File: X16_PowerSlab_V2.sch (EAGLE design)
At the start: 41 parts, among them J1 CONN_796636-3, J2 CONN_796636-3, J3 CONN_ET60T

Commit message: updated board
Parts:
- removed COUT1, COUT2, COUT3: 150uF, SparkFun-Capacitors:10UF-POLAR-0603-6.3V-20%(TANT)
- added COUT4, COUT5, COUT6: 150uF, X15-Conversion-Parts-Library:C-TANTALUM(10UF_150UF)
- CIN1: value 180uF -> 150uF; device SparkFun-Capacitors:10UF-POLAR-0603-6.3V-20%(TANT) -> X15-Conversion-Parts-Library:C-TANTALUM(10UF_150UF)
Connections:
- net 5.2V: now also COUT4.+, COUT5.+, COUT6.+; no longer COUT1.+, COUT2.+, COUT3.+
- net GND: now also COUT4.-, COUT5.-, COUT6.-; no longer COUT1.-, COUT2.-, COUT3.-
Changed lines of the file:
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@@
 <part name="CIN2" library="SparkFun-Capacitors" library_urn="urn:adsk.eagle:library:510" deviceset="0.1UF" device="-0603-25V-(+80/-20%)" package3d_urn="urn:adsk.eagle:package:41385090/1" value="0.47uF"/>
 <part name="C2" library="SparkFun-Capacitors" library_urn="urn:adsk.eagle:library:510" deviceset="0.1UF" device="-0603-25V-(+80/-20%)" package3d_urn="urn:adsk.eagle:package:41385090/1" value="0.01uF"/>
-<part name="COUT1" library="SparkFun-Capacitors" library_urn="urn:adsk.eagle:library:510" deviceset="10UF-POLAR" device="-0603-6.3V-20%(TANT)" package3d_urn="urn:adsk.eagle:package:41385074/1" value="150uF"/>
-<part name="COUT2" library="SparkFun-Capacitors" library_urn="urn:adsk.eagle:library:510" deviceset="10UF-POLAR" device="-0603-6.3V-20%(TANT)" package3d_urn="urn:adsk.eagle:package:41385074/1" value="150uF"/>
-<part name="COUT3" library="SparkFun-Capacitors" library_urn="urn:adsk.eagle:library:510" deviceset="10UF-POLAR" device="-0603-6.3V-20%(TANT)" package3d_urn="urn:adsk.eagle:package:41385074/1" value="150uF"/>
-<part name="CIN1" library="SparkFun-Capacitors" library_urn="urn:adsk.eagle:library:510" deviceset="10UF-POLAR" device="-0603-6.3V-20%(TANT)" package3d_urn="urn:adsk.eagle:package:41385074/1" value="180uF"/>
 <part name="R1" library="SparkFun-Resistors" library_urn="urn:adsk.eagle:library:532" deviceset="RESISTOR" device="0603" package3d_urn="urn:adsk.eagle:package:41389018/1" value="1k"/>
 <part name="R2" library="SparkFun-Resistors" library_urn="urn:adsk.eagle:library:532" deviceset="RESISTOR" device="0603" package3d_urn="urn:adsk.eagle:package:41389018/1" value="3.32k"/>
@@
 <part name="TP6" library="SparkFun-Connectors" library_urn="urn:adsk.eagle:library:513" deviceset="TEST-POINT" device="3X5" package3d_urn="urn:adsk.eagle:package:38285/2"/>
 <part name="L1" library="X15-Conversion-Parts-Library" deviceset="HCMA1305" device="" package3d_urn="urn:adsk.eagle:package:24201702/2" value="15uH"/>
+<part name="COUT4" library="X15-Conversion-Parts-Library" deviceset="C-TANTALUM(10UF_150UF)" device="" package3d_urn="urn:adsk.eagle:package:25131320/3" value="150uF"/>
+<part name="COUT5" library="X15-Conversion-Parts-Library" deviceset="C-TANTALUM(10UF_150UF)" device="" package3d_urn="urn:adsk.eagle:package:25131320/3" value="150uF"/>
+<part name="COUT6" library="X15-Conversion-Parts-Library" deviceset="C-TANTALUM(10UF_150UF)" device="" package3d_urn="urn:adsk.eagle:package:25131320/3" value="150uF"/>
+<part name="CIN1" library="X15-Conversion-Parts-Library" deviceset="C-TANTALUM(10UF_150UF)" device="" package3d_urn="urn:adsk.eagle:package:25131320/3" value="150uF"/>
 </parts>
 <sheets>
@@
 <attribute name="VALUE" x="50.419" y="65.024" size="1.778" layer="96" font="vector" rot="R90"/>
 </instance>
-<instance part="COUT1" gate="G$1" x="66.04" y="50.8" smashed="yes">
-<attribute name="NAME" x="67.056" y="51.435" size="1.778" layer="95" font="vector"/>
-<attribute name="VALUE" x="67.056" y="46.609" size="1.778" layer="96" font="vector"/>
-</instance>
-<instance part="COUT2" gate="G$1" x="73.66" y="50.8" smashed="yes">
-<attribute name="NAME" x="74.676" y="51.435" size="1.778" layer="95" font="vector"/>
-<attribute name="VALUE" x="74.676" y="46.609" size="1.778" layer="96" font="vector"/>
-</instance>
-<instance part="COUT3" gate="G$1" x="81.28" y="50.8" smashed="yes">
-<attribute name="NAME" x="82.296" y="51.435" size="1.778" layer="95" font="vector"/>
-<attribute name="VALUE" x="82.296" y="46.609" size="1.778" layer="96" font="vector"/>
-</instance>
-<instance part="CIN1" gate="G$1" x="-60.96" y="66.04" smashed="yes">
-<attribute name="NAME" x="-59.944" y="66.675" size="1.778" layer="95" font="vector"/>
-<attribute name="VALUE" x="-59.944" y="61.849" size="1.778" layer="96" font="vector"/>
-</instance>
 <instance part="R1" gate="G$1" x="60.96" y="81.28" smashed="yes">
 <attribute name="NAME" x="60.96" y="82.804" size="1.778" layer="95" font="vector" align="bottom-center"/>
@@
 <attribute name="NAME" x="50.8" y="57.15" size="0.762" layer="95"/>
 <attribute name="VALUE" x="50.8" y="54.61" size="0.762" layer="96"/>
+</instance>
+<instance part="COUT4" gate="G$1" x="66.04" y="50.8" smashed="yes">
+<attribute name="NAME" x="67.056" y="51.435" size="0.762" layer="95"/>
+<attribute name="VALUE" x="67.056" y="46.609" size="0.762" layer="96"/>
+</instance>
+<instance part="COUT5" gate="G$1" x="73.66" y="50.8" smashed="yes">
+<attribute name="NAME" x="74.676" y="51.435" size="0.762" layer="95"/>
+<attribute name="VALUE" x="74.676" y="46.609" size="0.762" layer="96"/>
+</instance>
+<instance part="COUT6" gate="G$1" x="81.28" y="50.8" smashed="yes">
+<attribute name="NAME" x="82.296" y="51.435" size="0.762" layer="95"/>
+<attribute name="VALUE" x="82.296" y="46.609" size="0.762" layer="96"/>
+</instance>
+<instance part="CIN1" gate="G$1" x="-60.96" y="66.04" smashed="yes">
+<attribute name="NAME" x="-59.944" y="66.675" size="0.762" layer="95"/>
+<attribute name="VALUE" x="-59.944" y="61.849" size="0.762" layer="96"/>
 </instance>
 </instances>
@@
 <net name="5.2V" class="0">
 <segment>
-<pinref part="COUT1" gate="G$1" pin="+"/>
 <wire x1="66.04" y1="55.88" x2="73.66" y2="55.88" width="0.1524" layer="91"/>
 <wire x1="73.66" y1="55.88" x2="81.28" y2="55.88" width="0.1524" layer="91"/>
@@
 <wire x1="66.04" y1="53.34" x2="66.04" y2="55.88" width="0.1524" layer="91"/>
 <junction x="66.04" y="55.88"/>
-<pinref part="COUT2" gate="G$1" pin="+"/>
 <wire x1="73.66" y1="53.34" x2="73.66" y2="55.88" width="0.1524" layer="91"/>
 <junction x="73.66" y="55.88"/>
-<pinref part="COUT3" gate="G$1" pin="+"/>
 <wire x1="81.28" y1="53.34" x2="81.28" y2="55.88" width="0.1524" layer="91"/>
 <junction x="81.28" y="55.88"/>
@@
 <label x="86.36" y="55.88" size="1.778" layer="95" xref="yes"/>
 <pinref part="L1" gate="G$1" pin="2"/>
+<pinref part="COUT4" gate="G$1" pin="+"/>
+<pinref part="COUT5" gate="G$1" pin="+"/>
+<pinref part="COUT6" gate="G$1" pin="+"/>
 </segment>
 <segment>
@@
 <pinref part="CIN2" gate="G$1" pin="2"/>
 <wire x1="-48.26" y1="60.96" x2="-48.26" y2="43.18" width="0.1524" layer="91"/>
-<pinref part="CIN1" gate="G$1" pin="-"/>
 <wire x1="-60.96" y1="60.96" x2="-60.96" y2="43.18" width="0.1524" layer="91"/>
 <wire x1="-60.96" y1="43.18" x2="-48.26" y2="43.18" width="0.1524" layer="91"/>
-<pinref part="COUT3" gate="G$1" pin="-"/>
 <wire x1="-48.26" y1="43.18" x2="-27.94" y2="43.18" width="0.1524" layer="91"/>
 <wire x1="-27.94" y1="43.18" x2="-17.78" y2="43.18" width="0.1524" layer="91"/>
@@
 <wire x1="73.66" y1="43.18" x2="81.28" y2="43.18" width="0.1524" layer="91"/>
 <wire x1="81.28" y1="43.18" x2="81.28" y2="45.72" width="0.1524" layer="91"/>
-<pinref part="COUT1" gate="G$1" pin="-"/>
 <wire x1="66.04" y1="45.72" x2="66.04" y2="43.18" width="0.1524" layer="91"/>
 <junction x="66.04" y="43.18"/>
-<pinref part="COUT2" gate="G$1" pin="-"/>
 <wire x1="73.66" y1="45.72" x2="73.66" y2="43.18" width="0.1524" layer="91"/>
 <junction x="73.66" y="43.18"/>
@@
 <junction x="50.8" y="43.18"/>
 <label x="-17.78" y="40.64" size="1.778" layer="95" rot="R270" xref="yes"/>
+<pinref part="COUT4" gate="G$1" pin="-"/>
+<pinref part="COUT5" gate="G$1" pin="-"/>
+<pinref part="COUT6" gate="G$1" pin="-"/>
+<pinref part="CIN1" gate="G$1" pin="-"/>
 </segment>
 <segment>
@@
 <pinref part="CIN2" gate="G$1" pin="1"/>
 <wire x1="-48.26" y1="68.58" x2="-48.26" y2="71.12" width="0.1524" layer="91"/>
-<pinref part="CIN1" gate="G$1" pin="+"/>
 <wire x1="-60.96" y1="68.58" x2="-60.96" y2="71.12" width="0.1524" layer="91"/>
 <pinref part="U$2" gate="G$1" pin="VIN"/>
@@
 <wire x1="-60.96" y1="71.12" x2="-68.58" y2="71.12" width="0.1524" layer="91"/>
 <pinref part="D4" gate="G$1" pin="C"/>
-</segment>
-</net>
+<pinref part="CIN1" gate="G$1" pin="+"/>
+</segment>
+</net>

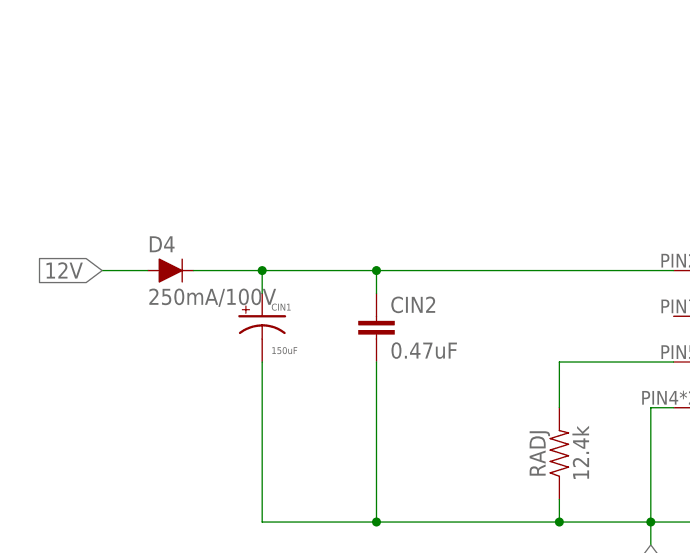
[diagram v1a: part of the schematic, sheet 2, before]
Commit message: finished polygons
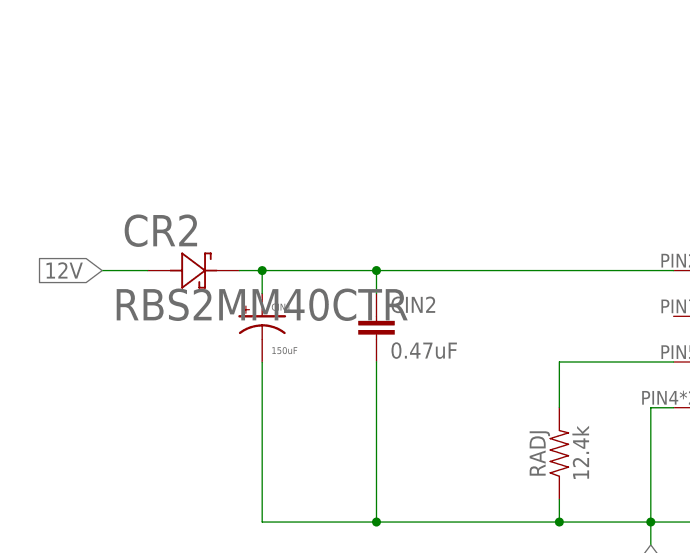
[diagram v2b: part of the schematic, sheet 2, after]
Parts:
- removed D4: 250mA/100V, SparkFun-DiscreteSemi:DIODE-BAS16J
- added CR2: RBS2MM40CTR, X16_Power_Slab:RBS2MM40CTR
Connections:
- net 12V: now also CR2.2; no longer D4.A
- net 48V_GND: now also U$3.RMCONT
- net VIN: now also CR2.1; no longer D4.C
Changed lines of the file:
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@@
 <part name="C4" library="SparkFun-Capacitors" library_urn="urn:adsk.eagle:library:510" deviceset="10UF-POLAR" device="-0603-6.3V-20%(TANT)" package3d_urn="urn:adsk.eagle:package:41385074/1" value="330uF"/>
 <part name="C7" library="SparkFun-Capacitors" library_urn="urn:adsk.eagle:library:510" deviceset="10UF-POLAR" device="-0603-6.3V-20%(TANT)" package3d_urn="urn:adsk.eagle:package:41385074/1" value="330uF"/>
-<part name="D4" library="SparkFun-DiscreteSemi" library_urn="urn:adsk.eagle:library:514" deviceset="DIODE" device="-BAS16J" package3d_urn="urn:adsk.eagle:package:38441/2" value="250mA/100V"/>
 <part name="U$6" library="X16_Power_Slab" deviceset="CONN_DISTRIBUTION_TO_CONVERSION" device=""/>
 <part name="48_TP" library="SparkFun-Connectors" library_urn="urn:adsk.eagle:library:513" deviceset="TEST-POINT" device="3X5" package3d_urn="urn:adsk.eagle:package:38285/2"/>
@@
 <part name="COUT6" library="X15-Conversion-Parts-Library" deviceset="C-TANTALUM(10UF_150UF)" device="" package3d_urn="urn:adsk.eagle:package:25131320/3" value="150uF"/>
 <part name="CIN1" library="X15-Conversion-Parts-Library" deviceset="C-TANTALUM(10UF_150UF)" device="" package3d_urn="urn:adsk.eagle:package:25131320/3" value="150uF"/>
+<part name="CR2" library="X16_Power_Slab" deviceset="RBS2MM40CTR" device=""/>
 </parts>
 <sheets>
@@
 </segment>
 <segment>
-<wire x1="12.7" y1="137.16" x2="5.08" y2="137.16" width="0.1524" layer="91"/>
+<wire x1="12.7" y1="137.16" x2="7.62" y2="137.16" width="0.1524" layer="91"/>
 <pinref part="U$3" gate="G$1" pin="48V_GND"/>
 <label x="5.08" y="137.16" size="1.778" layer="95"/>
+<pinref part="U$3" gate="G$1" pin="RMCONT"/>
+<wire x1="7.62" y1="137.16" x2="5.08" y2="137.16" width="0.1524" layer="91"/>
+<wire x1="12.7" y1="147.32" x2="7.62" y2="147.32" width="0.1524" layer="91"/>
+<wire x1="7.62" y1="147.32" x2="7.62" y2="137.16" width="0.1524" layer="91"/>
+<junction x="7.62" y="137.16"/>
 </segment>
 <segment>
@@
 <attribute name="VALUE" x="27.432" y="-3.175" size="1.778" layer="96" font="vector" rot="R180" align="top-left"/>
 </instance>
-<instance part="D4" gate="G$1" x="-71.12" y="71.12" smashed="yes">
-<attribute name="NAME" x="-73.66" y="73.152" size="1.778" layer="95" font="vector"/>
-<attribute name="VALUE" x="-73.66" y="69.088" size="1.778" layer="96" font="vector" align="top-left"/>
-</instance>
 <instance part="48_TP" gate="G$1" x="73.66" y="7.62" smashed="yes">
 <attribute name="NAME" x="71.12" y="10.16" size="1.778" layer="95" font="vector"/>
@@
 <attribute name="NAME" x="-59.944" y="66.675" size="0.762" layer="95"/>
 <attribute name="VALUE" x="-59.944" y="61.849" size="0.762" layer="96"/>
+</instance>
+<instance part="CR2" gate="A" x="-73.66" y="71.12" smashed="yes">
+<attribute name="VALUE" x="-77.5462" y="65.5828" size="3.4798" layer="96" ratio="10" rot="SR0"/>
+<attribute name="NAME" x="-76.4794" y="73.8124" size="3.4798" layer="95" ratio="10" rot="SR0"/>
 </instance>
 </instances>
@@
 <wire x1="-73.66" y1="71.12" x2="-78.74" y2="71.12" width="0.1524" layer="91"/>
 <label x="-78.74" y="71.12" size="1.778" layer="95" rot="R180" xref="yes"/>
-<pinref part="D4" gate="G$1" pin="A"/>
+<pinref part="CR2" gate="A" pin="2"/>
 </segment>
 </net>
@@
 <pinref part="U$2" gate="G$1" pin="VIN"/>
 <wire x1="-60.96" y1="71.12" x2="-48.26" y2="71.12" width="0.1524" layer="91"/>
-<junction x="-60.96" y="71.12"/>
 <junction x="-48.26" y="71.12"/>
 <wire x1="-48.26" y1="71.12" x2="-15.24" y2="71.12" width="0.1524" layer="91"/>
-<wire x1="-60.96" y1="71.12" x2="-68.58" y2="71.12" width="0.1524" layer="91"/>
-<pinref part="D4" gate="G$1" pin="C"/>
 <pinref part="CIN1" gate="G$1" pin="+"/>
-</segment>
-</net>
+<pinref part="CR2" gate="A" pin="1"/>
+<wire x1="-63.5" y1="71.12" x2="-60.96" y2="71.12" width="0.1524" layer="91"/>
+<junction x="-60.96" y="71.12"/>
+</segment>
+</net>

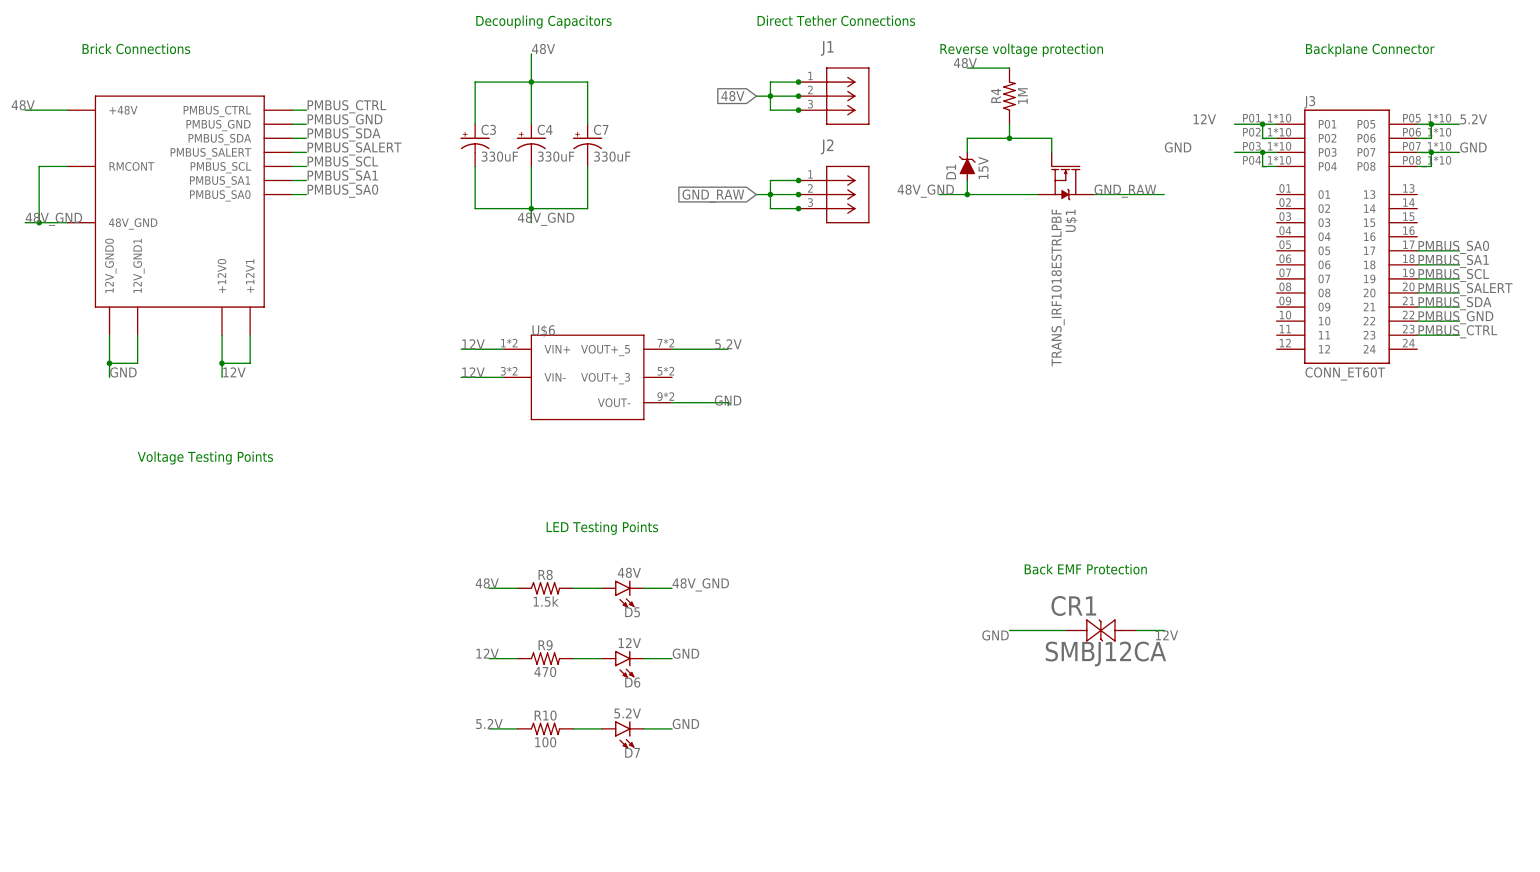
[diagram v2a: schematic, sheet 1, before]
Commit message: Followed video, few discrepancies
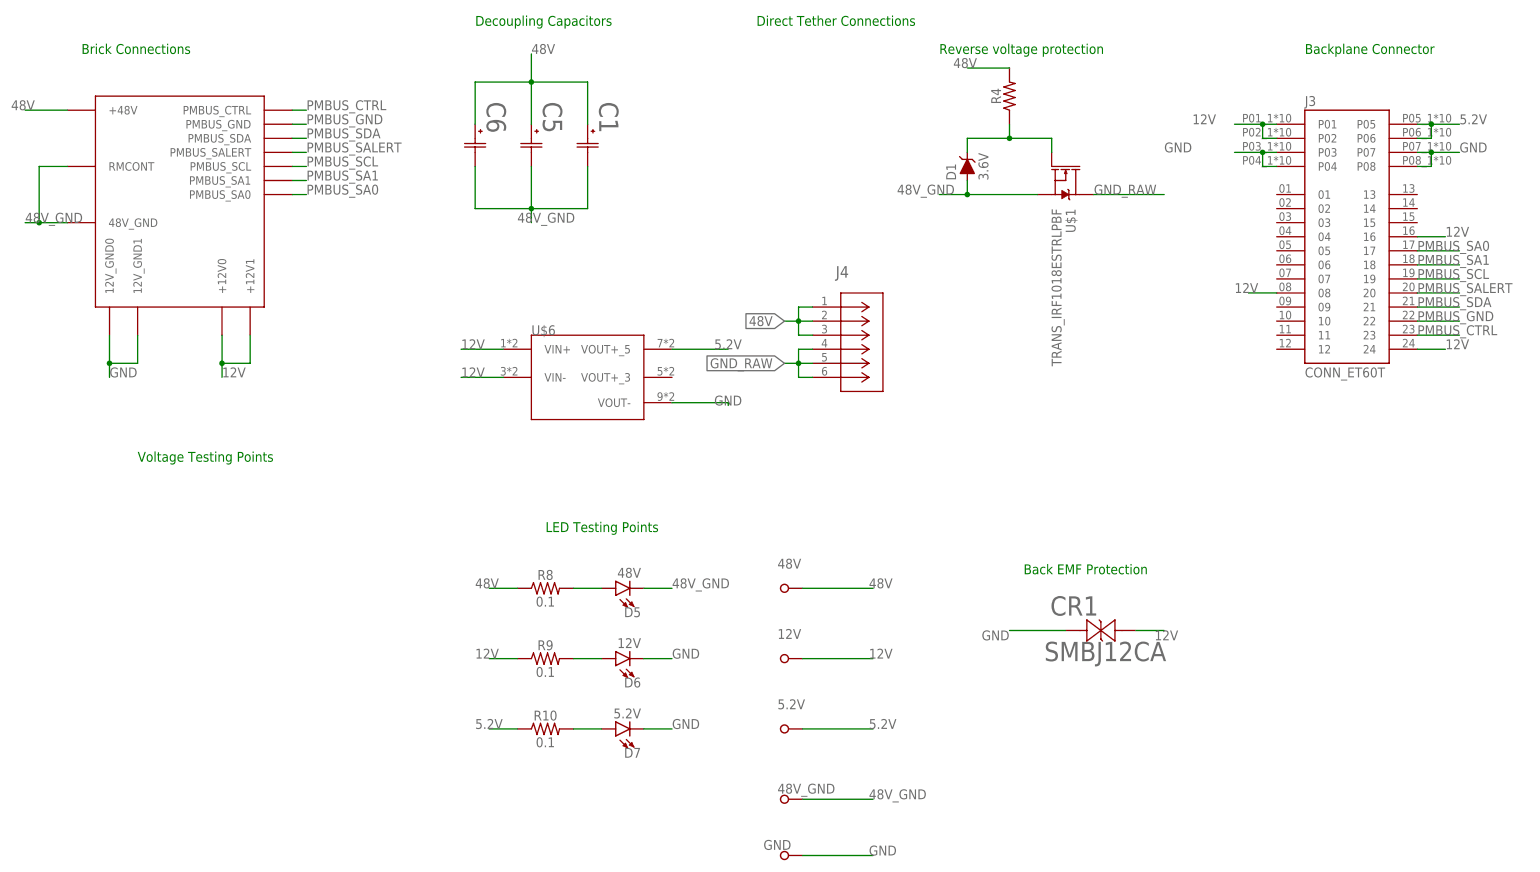
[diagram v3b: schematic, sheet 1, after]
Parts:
- removed 12VGND_TP, 12V_TP, 48VGND_TP, 48_TP, TP5, TP6: TEST-POINT3X5, SparkFun-Connectors:TEST-POINT3X5
- removed C3, C4, C7: 330uF, SparkFun-Capacitors:10UF-POLAR-0603-6.3V-20%(TANT)
- removed J1, J2: CONN_796636-3, X16_Power_Slab:CONN_796636-3
- added 12V, 48V_GND, 5.2V, GND: TESTPOINT_5.04MM, X16-ExtraComponents:TESTPOINT_5.04MM
- added 48V: 48V, X16-ExtraComponents:TESTPOINT_5.04MM
- added C1, C5, C6: UCM1H331MNL1GS, X16_Power_Slab:UCM1H331MNL1GS
- added J4: 796636-6, X16_Power_Slab:796636-6
- D1: value 15V -> 3.6V
- R1: value 1k -> (none)
- R10: value 100 -> 0.1
- R2: value 3.32k -> (none)
- R4: value 1M -> (none)
- R5: value 600 -> (none)
- R6: value 300 -> (none)
- R8: value 1.5k -> 0.1
- R9: value 470 -> 0.1
- RADJ: value 12.4k -> (none)
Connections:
- net 12V: now also 12V.TP, J3.08, J3.16, J3.24
- net 48V: now also 48V.TP, C1.1, C5.1, C6.1, J4.1, J4.2, J4.3; no longer C3.+, C4.+, C7.+, J1.1, J1.2, J1.3
- net 48V_GND: now also 48V_GND.TP, C1.2, C5.2, C6.2; no longer C3.-, C4.-, C7.-
- net 5.2V: now also 5.2V.TP
- net GND: now also GND.TP
- net GND_RAW: now also J4.4, J4.5, J4.6; no longer J2.1, J2.2, J2.3

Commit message: Labels added
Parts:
- D2, D3, D5, D6, D7: device SparkFun-LED:LED0603 -> SparkFun-LED:LED-RED-0805
- renumbered 12V to 12V_TP, 48V to 48V_TP, 48V_GND to 48V_GND_TP, 5.2V to 5.2V_TP, CR1 to BACK_EMF, DIODE to 40V_DIODE, GND to GND_TP, J3 to BACKPLANE_CONN, U$1 to TRANS_REVERSE_VOLT_PROTEC, U$3 to BMR480_POWERBRICK
